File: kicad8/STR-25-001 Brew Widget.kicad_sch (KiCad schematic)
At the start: 0 parts

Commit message: changes before bed
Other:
- added sheet ESP32 (ESP32.kicad_sch)
- added sheet Power Supply and Charging (Power_sch.kicad_sch)
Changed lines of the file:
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@@
 		(comment 3 "License: CC-A-SA")
+	)
+	(sheet
+		(at 127.254 56.388)
+		(size 24.384 17.526)
+		(fields_autoplaced yes)
+		(stroke
+			(width 0.1524)
+			(type solid)
+		)
+		(fill
+			(color 0 0 0 0.0000)
+		)
+		(property "Sheetname" "Power Supply and Charging"
+			(at 127.254 55.6764 0)
+			(effects
+				(font
+					(size 1.27 1.27)
+				)
+				(justify left bottom)
+			)
+		)
+		(property "Sheetfile" "Power_sch.kicad_sch"
+			(at 127.254 74.4986 0)
+			(effects
+				(font
+					(size 1.27 1.27)
+				)
+				(justify left top)
+			)
+		)
+		(instances
+			(project "STR-25-001 Brew Widget"
+				(path "/1376bbaf-6e04-46c3-997e-a362578a2a34"
+					(page "2")
+				)
+			)
+		)
+	)
+	(sheet
+		(at 127.254 83.058)
+		(size 24.638 16.256)
+		(fields_autoplaced yes)
+		(stroke
+			(width 0.1524)
+			(type solid)
+		)
+		(fill
+			(color 0 0 0 0.0000)
+		)
+		(property "Sheetname" "ESP32"
+			(at 127.254 82.3464 0)
+			(effects
+				(font
+					(size 1.27 1.27)
+				)
+				(justify left bottom)
+			)
+		)
+		(property "Sheetfile" "ESP32.kicad_sch"
+			(at 127.254 99.8986 0)
+			(effects
+				(font
+					(size 1.27 1.27)
+				)
+				(justify left top)
+			)
+		)
+		(instances
+			(project "STR-25-001 Brew Widget"
+				(path "/1376bbaf-6e04-46c3-997e-a362578a2a34"
+					(page "3")
+				)
+			)
+		)
 	)
 	(sheet_instances

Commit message: Ready for Schematic Review
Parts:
- added BT1: 18650, symbol Device:Battery_Cell
- added C1, C7, C8: 4.7uF, JLCPCB-Kicad-Footprints:C_0402, symbol JLCPCB-Capacitors:0402,4.7uF
- added C10, C11, C14, C15, C2, C3, C4: 100nF, JLCPCB-Kicad-Footprints:C_0402, symbol JLCPCB-Capacitors:0402,100nF
- added C12, C5, C6: 10uF, JLCPCB-Kicad-Footprints:C_0402, symbol JLCPCB-Capacitors:0402,10uF
- added C13: 1uF, JLCPCB-Kicad-Footprints:C_0402, symbol JLCPCB-Capacitors:0402,1uF
- added C9: 10pF, JLCPCB-Kicad-Footprints:C_0402, symbol JLCPCB-Capacitors:0402,10pF
- added D1: SS14, JLCPCB-Kicad-Footprints:D_SMA, symbol JLCPCB-Diodes:Schottky,SS14
- added D2: Red, LED_SMD:LED_0603_1608Metric, symbol STR-LED:Red
- added D3: Green, LED_SMD:LED_0603_1608Metric, symbol STR-LED:Green
- added D4: MBR0530, Diode_SMD:D_SOD-123, symbol Diode:MBR0530
- added H1, H2, H3: ~, JLCPCB-Kicad-Footprints:Hole_Tooling_JLCPCB, symbol JLCPCB-Manufacturing:Tooling Hole, JLCPCB, 1.152mm
- added J1: Connector, USB-TYPE-C-16P, JLCPCB-Kicad-Footprints:TYPE-C-SMD_HX-TYPE-C-16PIN, symbol JLCPCB-Extended:Connector, USB-TYPE-C-16P
- added L1: 10uH,600mA, JLCPCB-Kicad-Footprints:L_0402, symbol STR_Inductors:10uH,_600mA
- added PN1: ~, JLCPCB-Kicad-Footprints:Part_Num_JLCPCB, symbol JLCPCB-Manufacturing:Part Number, JLCPCB, 0.8x0.15mm
- added Q1: IRLML6401, Package_TO_SOT_SMD:SOT-23, symbol STR-MOSFETS:IRLML6401
- added Q2: FS8205A, Package_TO_SOT_SMD:SOT-23-6, symbol STR-MOSFETS:FS8205A
- added R1, R2, R5, R8, R9: 10kΩ, JLCPCB-Kicad-Footprints:R_0402, symbol JLCPCB-Resistors:0402,10kΩ
- added R10: 100kΩ, JLCPCB-Kicad-Footprints:R_0402, symbol JLCPCB-Resistors:0402,100kΩ
- added R11, R12: 2kΩ, JLCPCB-Kicad-Footprints:R_0402, symbol JLCPCB-Resistors:0402,2kΩ
- added R13: 200kΩ, JLCPCB-Kicad-Footprints:R_0402, symbol JLCPCB-Resistors:0402,200kΩ
- added R14: 120kΩ, JLCPCB-Kicad-Footprints:R_0402, symbol JLCPCB-Resistors:0402,120kΩ
- added R15: 100Ω, JLCPCB-Kicad-Footprints:R_0402, symbol JLCPCB-Resistors:0402,100Ω
- added R16, R3, R4: 4.7kΩ, JLCPCB-Kicad-Footprints:R_0402, symbol JLCPCB-Resistors:0402,4.7kΩ
- added R17: 1kΩ, JLCPCB-Kicad-Footprints:R_0402, symbol JLCPCB-Resistors:0402,1kΩ
- added R6, R7: 5.1kΩ, JLCPCB-Kicad-Footprints:R_0402, symbol JLCPCB-Resistors:0402,5.1kΩ
- added S1, S2: Tactile Button, 160gf, JLCPCB-Kicad-Footprints:SW-SMD_4P-L5.1-W5.1-P3.70-LS6.5-TL-2, symbol JLCPCB-Connectors_Buttons:Tactile Button, 160gf
- added U1: ESP32-C3-MINI-1-N4, esp:ESP32-C3-MINI-1-N4, symbol STR-ESP32:ESP32-C3-MINI-1-N4
- added U2: TPS61040, JLCPCB-Kicad-Footprints:SOT-23-5_L3.0-W1.7-P0.95-LS2.8-BL, symbol JLCPCB-Power:DC-DC, Boost, 1.8-6VIN, 0.4A, 28V-VOUT
- added U3: TP4057, Package_TO_SOT_SMD:TSOT-23-6, symbol STR-BatteryManagement:TP4057
- added U4: MPU-6500, Sensor_Motion:InvenSense_QFN-24_3x3mm_P0.4mm_NoMask, symbol STR-Sensors:MPU-6500
- added U5: MAX17048, easyeda2kicad:DFN-8_L2.0-W2.0-P0.50-BL-EP, symbol STR-BatteryManagement:MAX17048
- added U6: DS18B20U, Package_SO:MSOP-8_3x3mm_P0.65mm, symbol Sensor_Temperature:DS18B20U
- added U7: DW01A, Package_TO_SOT_SMD:SOT-23-6, symbol Battery_Management:DW01A
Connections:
- new net: C10.1, U4.10 (REGOUT)
- new net: D4.2 (A), L1.2, U2.1 (SW)
- new net: D3.1 (K), U3.5 (STDBY)
- new net: D2.2 (A), D3.2 (A), R11.2
- new net: BT1.2 (-), C15.2, Q2.1 (S1), U7.6 (GND)
- new net: Q2.4 (G2), U7.3 (OC)
- new net: Q2.6 (G1), U7.1 (OD)
- new net: C7.1, D1.1, L1.1, Q1.2 (S), U2.4 (EN), U2.5 (VIN)
- new net: J1.A5 (CC1), R6.1
- new net: C9.2, R13.2, R14.1, U2.3 (FB)
- new net: U1.10 (NC), U1.15 (NC), U1.17 (NC), U1.24 (NC), U1.25 (NC), U1.28 (NC), U1.29 (NC), U1.32 (NC), U1.33 (NC), U1.34 (NC), U1.35 (NC), U1.4 (NC), U1.7 (NC), U1.9 (NC)
- new net: U1.11 (GND), U1.14 (GND), U1.2 (GND), U1.36 (GND), U1.37 (GND), U1.38 (GND), U1.39 (GND), U1.40 (GND), U1.41 (GND), U1.42 (GND), U1.43 (GND), U1.44 (GND), U1.45 (GND), U1.46 (GND), U1.47 (GND), U1.48 (GND), U1.50 (GND), U1.51 (GND), U1.52 (GND), U1.53 (GND)
- new net: R9.2, U1.22 (IO8)
- new net: U1.49_2 (GND_THERMAL), U1.49_3 (GND_THERMAL), U1.49_4 (GND_THERMAL), U1.49_5 (GND_THERMAL), U1.49_6 (GND_THERMAL), U1.49_7 (GND_THERMAL), U1.49_8 (GND_THERMAL), U1.49_9 (GND_THERMAL)
- new net: R2.2, U1.5 (IO2)
- new net: J1.B5 (CC2), R7.1
- new net: C15.1, R15.2, U7.5 (VCC)
- new net: R12.1, U3.6 (PROG)
- new net: R17.1, U7.2 (CS)
- new net: D2.1 (K), U3.1 (~{CHRG})
- new net +3.3V: C11.1, C13.1, C4.1, C5.1, C6.1, C9.1, D4.1 (K), R1.1, R13.1, R16.1, R2.1, R3.1, R4.1, R5.1, R8.1, R9.1, U1.3 (3V3), U4.13 (VDD), U4.22 (nCS), U4.8 (VDDIO), U6.8 (V_{DD})
- new net +BATT: BT1.1 (+), C12.1, C14.1, Q1.3 (D), R15.1, U3.3 (BAT), U5.2 (CELL), U5.3 (VDD)
- new net -BATT: C1.2, C10.2, C11.2, C12.2, C13.2, C14.2, C2.2, C3.2, C4.2, C5.2, C6.2, C7.2, C8.2, J1.A12B1 (GND), J1.B12A1 (GND), J1.S1 (SHIELD), Q2.3 (S2), R10.2, R12.2, R14.2, R17.2, R6.2, R7.2, S1.1 (A), S1.2 (B), S2.1 (A), S2.2 (B), U1.1 (GND), U1.49 (GND_THERMAL), U2.2 (GND), U3.2 (GND), U4.11 (FSYNC), U4.18 (GND), U4.20 (RESV), U4.9 (AD0), U5.1 (CTG), U5.4 (GND), U5.6 (QSTRT), U5.9 (EP), U6.4 (GND)
- new net EN: C1.1, C3.1, R1.2, R8.2, S2.3 (C), S2.4 (D), U1.8 (EN)
- new net GPIO9: C2.1, R5.2, S1.3 (C), S1.4 (D), U1.23 (IO9)
- new net SCA: R4.2, U1.6 (IO3), U4.23 (SCL)
- new net SCL: R3.2, U1.18 (IO4), U4.24 (SDA), U5.7 (SCL)
- new net SDA: U5.8 (SDA)
- new net TEMP: R16.2, U1.13 (IO1), U6.1 (DQ)
- new net USB_D+: J1.A6 (D+), J1.B6 (D+), U1.27 (IO19)
- new net USB_D-: J1.A7 (D-), J1.B7 (D-), U1.26 (IO18)
- new net VBUS: C8.1, D1.2, J1.A9B4 (VBUS), J1.B9A4 (VBUS), Q1.1 (G), R10.1, R11.1, U3.4 (V_{CC})
- new net ~{BAT_ALERT}: U1.12 (IO0), U5.5 (~{ALRT})
- no-connect marks 0 -> 13
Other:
- removed sheet ESP32
- removed sheet Power Supply and Charging
- note added: "1.233v"
- note added: "4.2V 500mA charge"
- note added: "400mA"
- note added: "Battery Charger"
- note added: "Battery Guage"
- note added: "Battery Protection"
- note added: "Boot"
- note added: "Buttons"
- note added: "DCDC Regulator"
- note added: "I2C Pullup"
- note added: "JLPCB Manufacturing"
- note added: "Reset"
- note added: "Temperature Sensor"
- note added: "Tilt Sensor-Accelerometer/Gyro"
- note added: "USB-C"
- note added: "VIN: 2.9-5V VOUT: 3.3V@400mA"
- note added: "Vout = 1.233 * ( 1 + ( 200K / 120K)) = 3.288v"

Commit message: Started PCB Layout
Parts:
- removed D1: SS14, JLCPCB-Kicad-Footprints:D_SMA, symbol JLCPCB-Diodes:Schottky,SS14
- removed D4: MBR0530, Diode_SMD:D_SOD-123, symbol Diode:MBR0530
- removed J1: Connector, USB-TYPE-C-16P, JLCPCB-Kicad-Footprints:TYPE-C-SMD_HX-TYPE-C-16PIN, symbol JLCPCB-Extended:Connector, USB-TYPE-C-16P
- removed R6, R7: 5.1kΩ, JLCPCB-Kicad-Footprints:R_0402, symbol JLCPCB-Resistors:0402,5.1kΩ
- removed S1, S2: Tactile Button, 160gf, JLCPCB-Kicad-Footprints:SW-SMD_4P-L5.1-W5.1-P3.70-LS6.5-TL-2, symbol JLCPCB-Connectors_Buttons:Tactile Button, 160gf
- added D1, D4: B16WS, JLCPCB-Kicad-Footprints:D_SOD-323, symbol JLCPCB-Diodes:Schottky,B16WS
- added J1: USB_B_Micro, STR-USB:USB_Micro-B_C319160, symbol STR-USB:USB_B_Micro
- added R15: 0Ω, JLCPCB-Kicad-Footprints:R_0402, symbol JLCPCB-Resistors:0402,0Ω
- added R17: 10kΩ, JLCPCB-Kicad-Footprints:R_0402, symbol JLCPCB-Resistors:0402,10kΩ
- added SW1, SW2: SW_MINI, STR-Switch:SW_SMD_SPST_8x3.6, symbol STR-Switches:SW_MINI
- BT1: footprint (none) -> Battery:BatteryHolder_Keystone_1042_1x18650
- L1: footprint JLCPCB-Kicad-Footprints:L_0402 -> Inductor_SMD:L_Wuerth_WE-GF-1210
- U1: footprint esp:ESP32-C3-MINI-1-N4 -> STR-ESP32:ESP32-C3-MINI-1-N4
- U6: renamed from U5; footprint easyeda2kicad:DFN-8_L2.0-W2.0-P0.50-BL-EP -> Package_DFN_QFN:TDFN-8-1EP_2x2mm_P0.5mm_EP0.8x1.2mm
- renumbered C2 to C1, C1 to C2, R2 to R1, R12 to R10, R13 to R11, R14 to R12, R16 to R13, R15 to R14, R17 to R16, R5 to R2, R1 to R3, R8 to R4, R3 to R5, R4 to R6, R9 to R7, R10 to R8, R11 to R9, U6 to U5
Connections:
- net +3.3V: now also D4.1, R17.1
- net -BATT: now also R15.1; no longer C1.2, C10.2, C11.2, C12.2, C13.2, C2.2, C3.2, C4.2, C5.2, C6.2, C7.2, C8.2, R10.2, R12.2, R8.2, U1.1 (GND), U1.49 (GND_THERMAL), U2.2 (GND), U3.2 (GND), U4.11 (FSYNC), U4.18 (GND), U4.20 (RESV), U4.9 (AD0), U5.4 (GND)
- net EN: now also SW2.2
- net GPIO9: now also SW1.2
- net SCA: now also U4.24 (SDA); no longer U4.23 (SCL)
- net SCL: now also U4.23 (SCL); no longer U4.24 (SDA)
- net USB_D+: now also J1.3 (D+)
- net USB_D-: now also J1.2 (D-)
- net VBUS: now also D1.2, J1.1 (VBUS)
- net ~{BAT_ALERT}: now also R17.2
- net at L1.2, U2.1 (SW): now also D4.2
- net -BATT_NOPROT: now reaches BT1.2 (-), C15.2, Q2.1 (S1), U7.6 (GND)
- net at C7.1, L1.1, Q1.2 (S)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: now also D1.1
- net GND: now reaches U1.11 (GND), U1.14 (GND), U1.2 (GND), U1.36 (GND), U1.37 (GND), U1.38 (GND), U1.39 (GND), U1.40 (GND), U1.41 (GND), U1.42 (GND), U1.43 (GND), U1.44 (GND), U1.45 (GND), U1.46 (GND), U1.47 (GND), U1.48 (GND), U1.50 (GND), U1.51 (GND), U1.52 (GND), U1.53 (GND)
- net GND: now also C1.2, C10.2, C11.2, C12.2, C13.2, C2.2, C3.2, C4.2, C5.2, C6.2, C7.2, C8.2, R10.2, R12.2, R8.2, U1.1 (GND), U1.49 (GND_THERMAL), U1.49_2 (GND_THERMAL), U1.49_3 (GND_THERMAL), U1.49_4 (GND_THERMAL), U1.49_5 (GND_THERMAL), U1.49_6 (GND_THERMAL), U1.49_7 (GND_THERMAL), U1.49_8 (GND_THERMAL), U1.49_9 (GND_THERMAL), U2.2 (GND), U3.2 (GND), U4.11 (FSYNC), U4.18 (GND), U4.20 (RESV), U4.9 (AD0), U5.4 (GND), J1.5 (GND), J1.6 (Shield), R15.2, SW1.1, SW2.1
- no-connect marks 13 -> 12
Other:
- note added: "ESP32"
- note added: "I2C"
- note added: "USB"
- note removed: "USB-C"
- moved on the sheet: C1, C2, C3, C4, C5, R1, R13, R2, R3, R4, R5, R6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

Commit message: PCB routed and all 3d models correct, needs final review
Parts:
- removed C13: 1uF, JLCPCB-Kicad-Footprints:C_0402, symbol JLCPCB-Capacitors:0402,1uF
- removed C7: 4.7uF, JLCPCB-Kicad-Footprints:C_0402, symbol JLCPCB-Capacitors:0402,4.7uF
- removed H1, H2, H3: ~, JLCPCB-Kicad-Footprints:Hole_Tooling_JLCPCB, symbol JLCPCB-Manufacturing:Tooling Hole, JLCPCB, 1.152mm
- removed L1: 10uH,600mA, Inductor_SMD:L_Wuerth_WE-GF-1210, symbol STR_Inductors:10uH,_600mA
- removed R11: 200kΩ, JLCPCB-Kicad-Footprints:R_0402, symbol JLCPCB-Resistors:0402,200kΩ
- removed R12: 120kΩ, JLCPCB-Kicad-Footprints:R_0402, symbol JLCPCB-Resistors:0402,120kΩ
- removed U2: TPS61040, JLCPCB-Kicad-Footprints:SOT-23-5_L3.0-W1.7-P0.95-LS2.8-BL, symbol JLCPCB-Power:DC-DC, Boost, 1.8-6VIN, 0.4A, 28V-VOUT
- added C10, C16: 100pF, JLCPCB-Kicad-Footprints:C_0402, symbol JLCPCB-Capacitors:0402,100pF
- added C17, C9: 1uF, JLCPCB-Kicad-Footprints:C_0402, symbol JLCPCB-Capacitors:0402,1uF
- added C18, C19, C7, C8: 10uF, JLCPCB-Kicad-Footprints:C_0402, symbol JLCPCB-Capacitors:0402,10uF
- added L1: 22uH,540mA, STR-Passive:IND_LQH3NPZ220MMEL, symbol STR_Inductors:22uH,540mA
- added R11: 68kΩ, JLCPCB-Kicad-Footprints:R_0402, symbol JLCPCB-Resistors:0402,68kΩ
- added R12: 15kΩ, JLCPCB-Kicad-Footprints:R_0402, symbol JLCPCB-Resistors:0402,15kΩ
- added TP1, TP2, TP3, TP4, TP5, TP6, TP7, TP8: TestPoint, TestPoint:TestPoint_Pad_D2.0mm, symbol Connector:TestPoint
- added TP10, TP11: TestPoint, TestPoint:TestPoint_Pad_D1.0mm, symbol Connector:TestPoint
- added TP9: TestPoint, TestPoint:TestPoint_Pad_2.5x2.5mm, symbol Connector:TestPoint
- added U3: MT3608, Package_TO_SOT_SMD:SOT-23-6, symbol Regulator_Switching:MT3608
- BT1: LCSC (none) -> C5249310; MFN (none) -> Keystone; MFPN (none) -> 1042
- D2: value Red -> CHG
- D3: value Green -> STBY
- J1: footprint STR-USB:USB_Micro-B_C319160 -> Connector_USB:USB_Micro-B_Molex_47346-0001
- SW1: value SW_MINI -> BOOT
- SW2: value SW_MINI -> RESET
- renumbered C8 to C11, C10 to C12, C9 to C13, C11 to C14, C12 to C15, C14 to C20, C15 to C21, R14 to R13, R13 to R14, R17 to R15, R15 to R16, R16 to R17, U3 to U2, U6 to U5, U5 to U6
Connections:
- net SCA is gone; now on net SDA: R6.2, U1.6 (IO3), U4.24 (SDA)
- net +3.3V: now also C16.1, C17.1, C18.1, C19.1, R11.1, TP3.1
- net +BATT: now also TP4.1
- net -BATT: now also TP8.1
- net GND: now also C10.2, C16.2, C17.2, C18.2, C19.2, C7.2, C8.2, C9.2, R12.2, TP9.1, U3.2 (GND)
- net SCL: now also TP7.1
- net SDA: now also TP6.1
- net TEMP: now also TP5.1
- net USB_D+: now also TP10.1
- net USB_D-: now also TP11.1
- net VBUS: now also TP1.1
- net VIN: now reaches D1.1, Q1.2 (S)
- net VIN: now also C10.1, C7.1, C8.1, C9.1, L1.1, TP2.1, U3.4 (EN), U3.5 (IN)
- net FB: now reaches C13.2
- net FB: now also R11.2, R12.1, U3.3 (FB)
- net VOUT: now reaches D4.2
- net VOUT: now also L1.2, U3.1 (SW)
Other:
- note added: "0.6v"
- note added: "VIN: 2.9-5V VOUT: 3.3V@1.2A"
- note added: "Vout = 0.6 * ( 1 + ( 68K / 15K)) = 3.32v"
- note removed: "1.233v"
- note removed: "400mA"
- note removed: "VIN: 2.9-5V VOUT: 3.3V@400mA"
- note removed: "Vout = 1.233 * ( 1 + ( 200K / 120K)) = 3.288v"
- moved on the sheet: C12, C13, C14, C20, C6, D1, D4, PN1, Q1, R14, R15, R16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

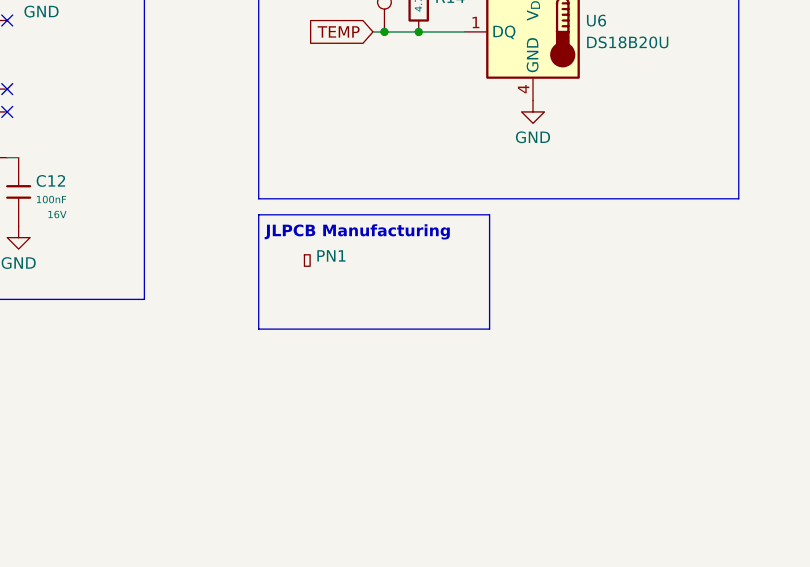
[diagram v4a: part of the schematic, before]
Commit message: Added Fiducals
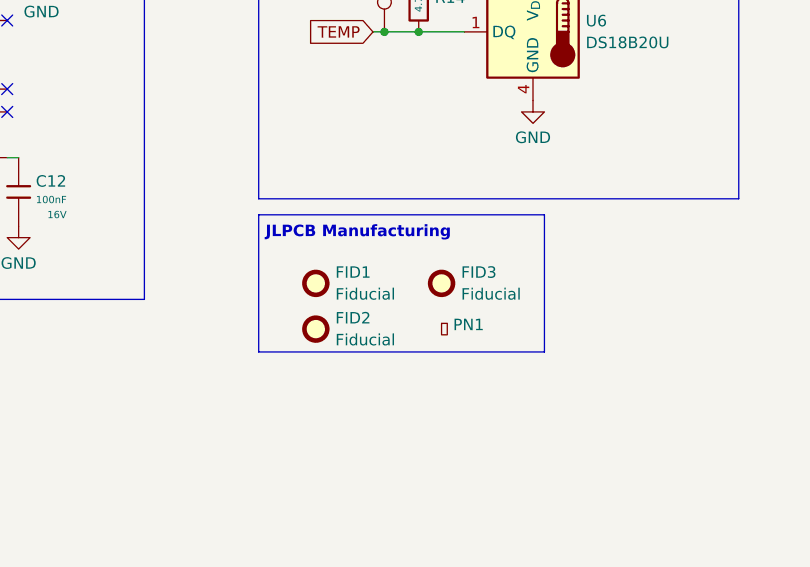
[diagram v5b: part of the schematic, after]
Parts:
- added FID1, FID2, FID3: Fiducial, Fiducial:Fiducial_0.5mm_Mask1mm, symbol Mechanical:Fiducial
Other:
- moved on the sheet: PN1
